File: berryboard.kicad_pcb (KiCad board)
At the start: 2 copper layers, 56 x 65 mm, 51 parts, among them J1 XT30_SERVO_PWR, J10 SERVO_7, J11 SERVO_8, J12 QWIIC_RPI_1, J13 QWIIC_RPI_2, J14 QWIIC_RPI_3, J15 QWIIC_MCU_1, J16 QWIIC_MCU_2, J17 QWIIC_MCU_3, J18 LEAK_1, J19 LEAK_2, J2 RPi_GPIO_40P, J20 HAT_5V_IN, J21 SWD, J3 USB_C_RP2350, J4 SERVO_1, J5 SERVO_2, J6 SERVO_3, J7 SERVO_4, J8 SERVO_5, J9 SERVO_6, U1 TPS2121, U2 AP2112K-3.3, U3 ICM-42688-P, U4 MMC5983MA, U5 24LC32, U6 RP2350B, U7 W25Q16JVSS

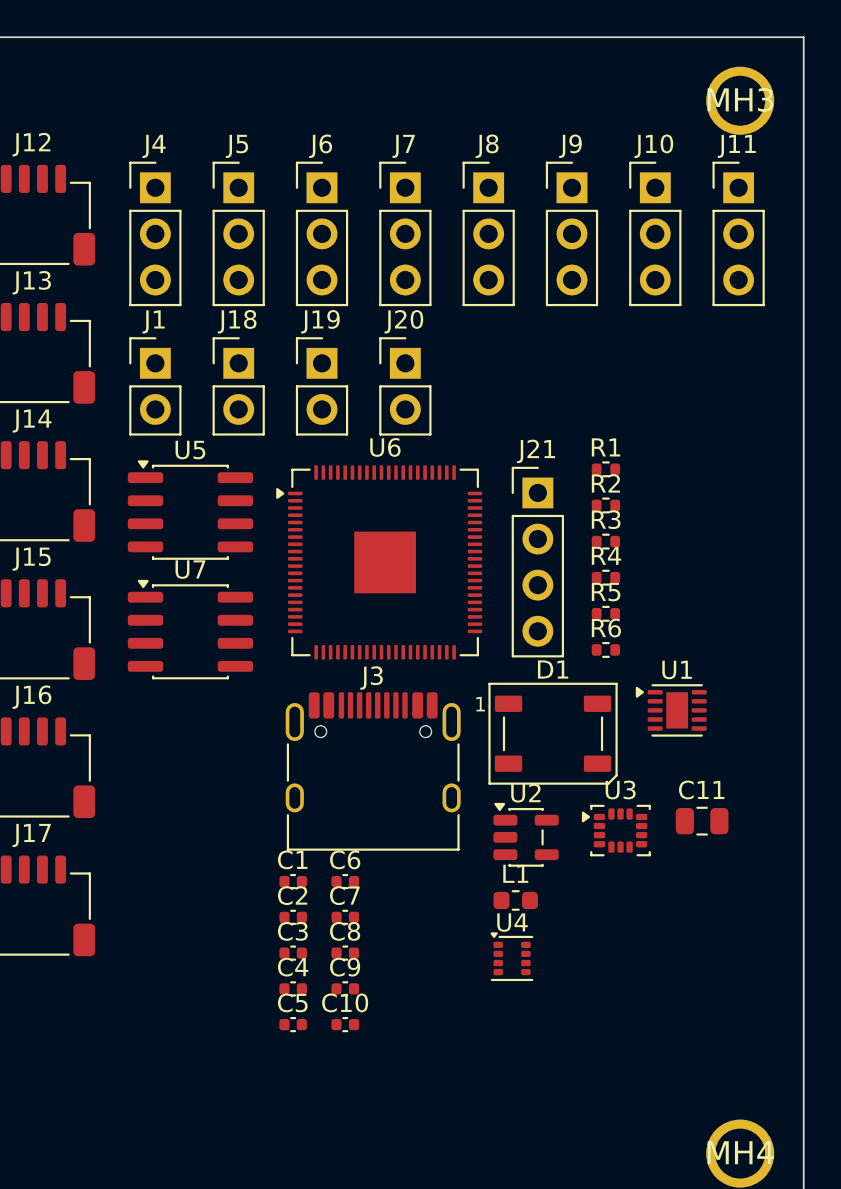
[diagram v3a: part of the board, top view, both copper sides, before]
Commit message: Update PCB: remove old servo connectors, add 3x 1x8 headers
Synced PCB from schematic after servo header redesign:
- Deleted J4–J11 footprints (eight 1x3 servo headers) from board
- Added J4 (SERVO_SIG), J5 (SERVO_PWR), J6 (SERVO_GND) as
  PinHeader_1x08_P2.54mm_Vertical footprints, ready for placement

Co-Authored-By: Claude Sonnet 4.6 <noreply@anthropic.com>
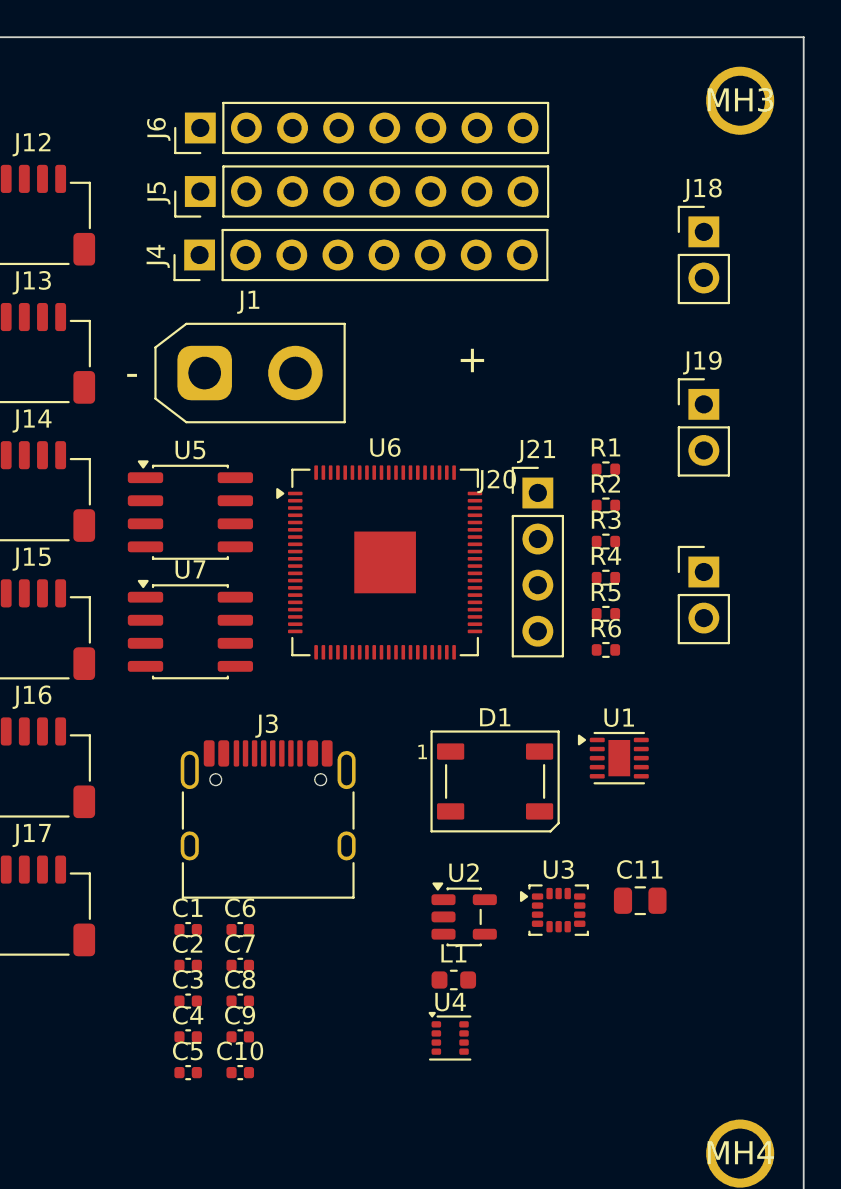
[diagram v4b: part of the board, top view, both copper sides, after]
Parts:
- removed J10: SERVO_7, Connector_PinHeader_2.54mm:PinHeader_1x03_P2.54mm_Vertical
- removed J11: SERVO_8, Connector_PinHeader_2.54mm:PinHeader_1x03_P2.54mm_Vertical
- removed J7: SERVO_4, Connector_PinHeader_2.54mm:PinHeader_1x03_P2.54mm_Vertical
- removed J8: SERVO_5, Connector_PinHeader_2.54mm:PinHeader_1x03_P2.54mm_Vertical
- removed J9: SERVO_6, Connector_PinHeader_2.54mm:PinHeader_1x03_P2.54mm_Vertical
- J1: footprint Connector_PinHeader_2.54mm:PinHeader_1x02_P2.54mm_Vertical -> Connector_AMASS:AMASS_XT30UPB-F_1x02_P5.0mm_Vertical
- J4: value SERVO_1 -> SERVO_SIG; footprint Connector_PinHeader_2.54mm:PinHeader_1x03_P2.54mm_Vertical -> Connector_PinHeader_2.54mm:PinHeader_1x08_P2.54mm_Vertical
- J5: value SERVO_2 -> SERVO_PWR; footprint Connector_PinHeader_2.54mm:PinHeader_1x03_P2.54mm_Vertical -> Connector_PinHeader_2.54mm:PinHeader_1x08_P2.54mm_Vertical
- J6: value SERVO_3 -> SERVO_GND; footprint Connector_PinHeader_2.54mm:PinHeader_1x03_P2.54mm_Vertical -> Connector_PinHeader_2.54mm:PinHeader_1x08_P2.54mm_Vertical
- moved J18 26.6 mm to (171.0, 83.2)
- moved J19 21.2 mm to (171.0, 92.7)
- moved J20 20.1 mm to (171.0, 102.0)
- moved J6 7.47 mm to (143.3, 77.5), turned to 90 degrees
- moved C1 6.36 mm to (142.6, 121.7)
- moved C10 6.36 mm to (145.5, 129.5)
- moved C2 6.36 mm to (142.6, 123.6)
- moved C3 6.36 mm to (142.6, 125.6)
- moved C4 6.36 mm to (142.6, 127.6)
- moved C5 6.36 mm to (142.6, 129.5)
- moved C6 6.36 mm to (145.5, 121.7)
- moved C7 6.36 mm to (145.5, 123.6)
- moved C8 6.36 mm to (145.5, 125.6)
- moved C9 6.36 mm to (145.5, 127.6)
- moved J3 6.36 mm to (147.0, 116.0)
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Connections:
- J4 pad 1: /SERVO_0 -> /SERVO_6
- J4 pad 2: /SERVO_PWR -> /SERVO_5
- J4 pad 3: /GND -> /SERVO_4
- J5 pad 1: /SERVO_1 -> /SERVO_PWR
- J5 pad 3: /GND -> /SERVO_PWR
- J6 pad 1: /SERVO_2 -> /GND
- J6 pad 2: /SERVO_PWR -> /GND

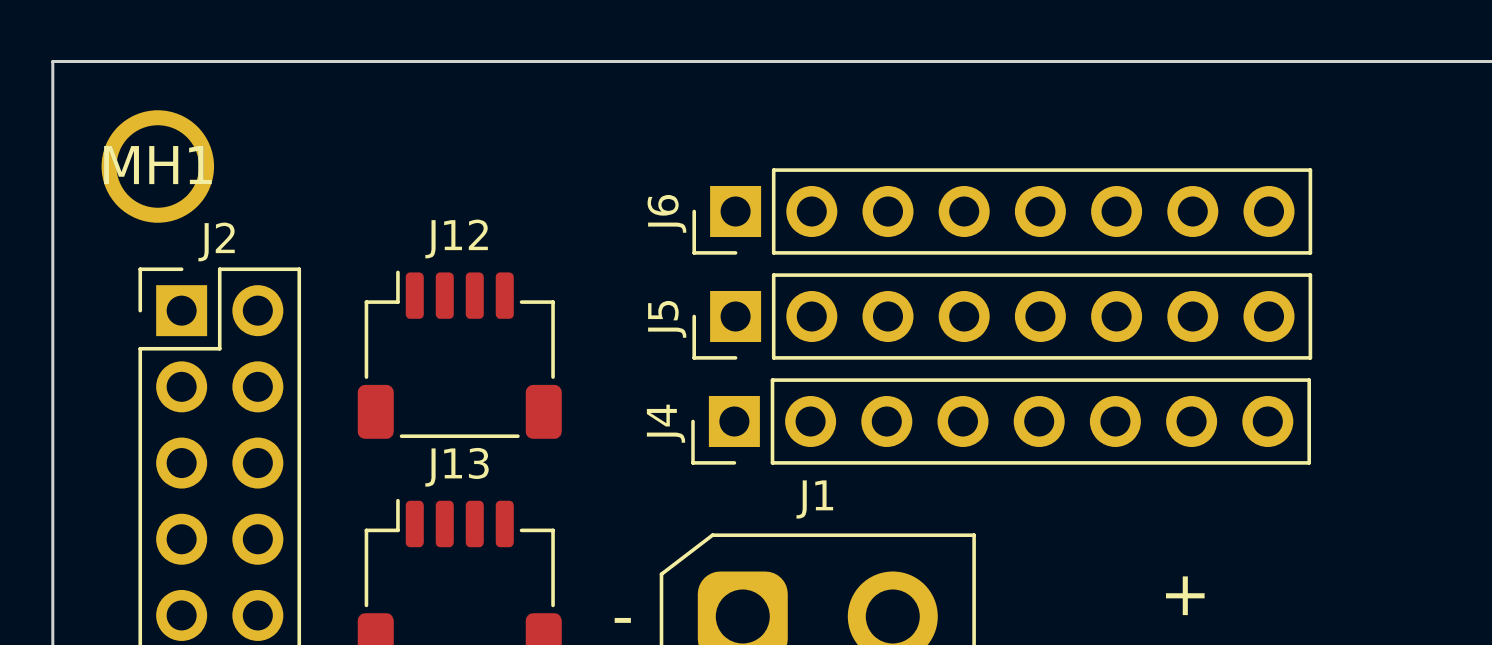
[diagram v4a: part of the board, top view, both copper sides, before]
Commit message: PCB: fix servo header spacing and order; schematic: add SERVO_PWR protection and SERVO_MON divider
PCB changes:
- Reorder J4/J5/J6 so signal (J4) is at top (y=77.5), power (J5) at y=80.04,
  ground (J6) at y=82.58 — matches yellow/red/black color convention
- Fix row spacing to exactly 2.54mm so a 3-pin Dupont housing mates all three
  rows simultaneously
- Align all three X coordinates to 143.22
- Add F.SilkS channel labels "1"–"8" above the servo header block

Schematic changes:
- Add D2 (SMBJ7.5A TVS diode) from SERVO_PWR to GND for transient protection
- Add C12 (100µF bulk capacitor) on SERVO_PWR for servo current decoupling
- Add R7/R8 (220k/100k) voltage divider: SERVO_PWR → SERVO_MON → GND,
  scaling up to 8.4V battery down to ≤2.6V for RP2350B ADC3 input
- U4 (MMC5983MA) footprint confirmed correct: OptoDevice:Broadcom_LGA-8_2x2mm_P0.5mm
  is the only matching 2×2mm / 0.5mm pitch LGA-8 in KiCad standard library
- U5 (24LC32) DNP flag confirmed already clear

Co-Authored-By: Claude Sonnet 4.6 <noreply@anthropic.com>
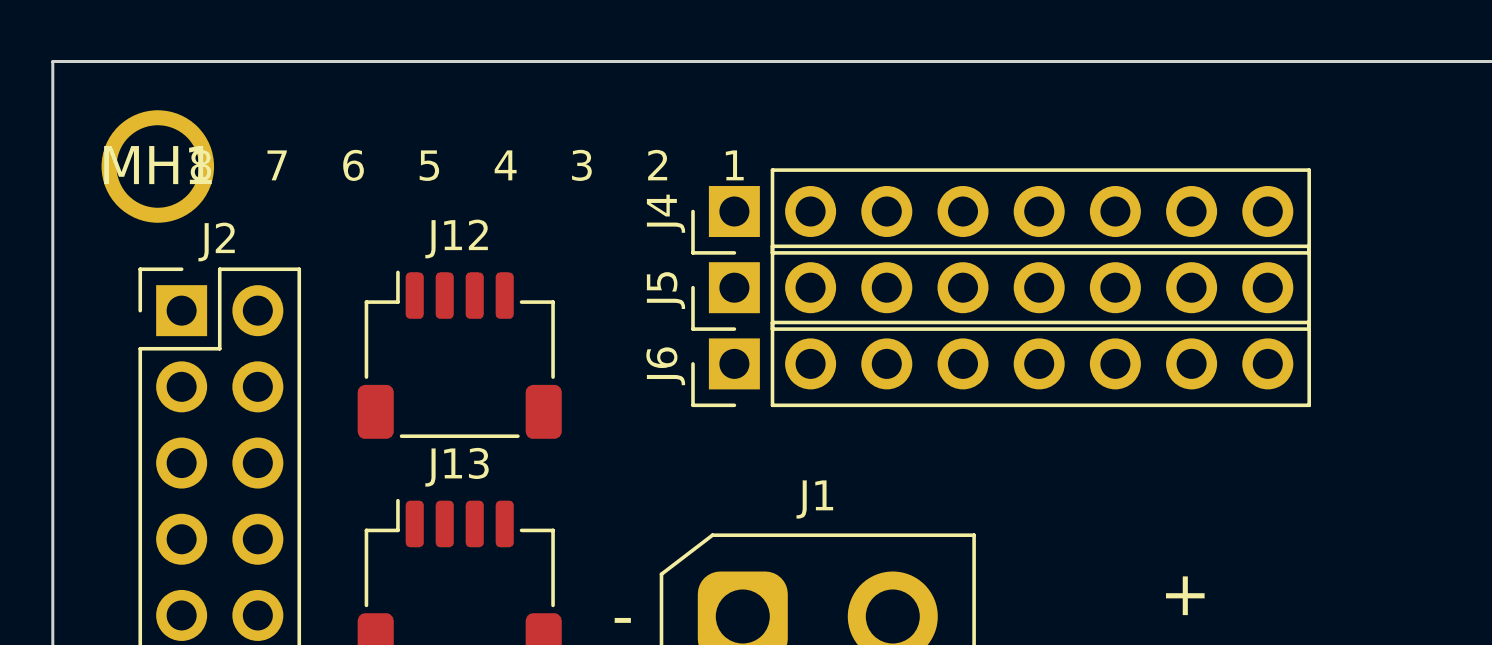
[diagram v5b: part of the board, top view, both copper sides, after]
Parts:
- moved J4 7.00 mm to (143.2, 77.5)
- moved J6 5.08 mm to (143.2, 82.6)
- moved J5 0.96 mm to (143.2, 80.0)
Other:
- board text added: "1"
- board text added: "2"
- board text added: "3"
- board text added: "4"
- board text added: "5"
- board text added: "6"
- board text added: "7"
- board text added: "8"
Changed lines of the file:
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@@
 	(footprint "Connector_PinHeader_2.54mm:PinHeader_1x08_P2.54mm_Vertical"
 		(layer "F.Cu")
-		(at 143.22 84.5 90)
+		(at 143.22 77.5 90)
 		(descr "Through hole straight pin header, 1x08, 2.54mm pitch, single row")
 		(tags "Through hole pin header THT 1x08 2.54mm single row")
@@
 	(footprint "Connector_PinHeader_2.54mm:PinHeader_1x08_P2.54mm_Vertical"
 		(layer "F.Cu")
-		(at 143.26 77.5 90)
+		(at 143.22 82.58 90)
 		(descr "Through hole straight pin header, 1x08, 2.54mm pitch, single row")
 		(tags "Through hole pin header THT 1x08 2.54mm single row")
@@
 	(footprint "Connector_PinHeader_2.54mm:PinHeader_1x08_P2.54mm_Vertical"
 		(layer "F.Cu")
-		(at 143.26 81 90)
+		(at 143.22 80.04 90)
 		(descr "Through hole straight pin header, 1x08, 2.54mm pitch, single row")
 		(tags "Through hole pin header THT 1x08 2.54mm single row")
@@
 		(layer "Edge.Cuts")
 	)
+	(gr_text "1"
+		(at 143.22 76)
+		(layer "F.SilkS")
+		(effects
+			(font
+				(size 1 1)
+				(thickness 0.15)
+			)
+			(justify center)
+		)
+	)
+	(gr_text "2"
+		(at 140.68 76)
+		(layer "F.SilkS")
+		(effects
+			(font
+				(size 1 1)
+				(thickness 0.15)
+			)
+			(justify center)
+		)
+	)
+	(gr_text "3"
+		(at 138.14 76)
+		(layer "F.SilkS")
+		(effects
+			(font
+				(size 1 1)
+				(thickness 0.15)
+			)
+			(justify center)
+		)
+	)
+	(gr_text "4"
+		(at 135.6 76)
+		(layer "F.SilkS")
+		(effects
+			(font
+				(size 1 1)
+				(thickness 0.15)
+			)
+			(justify center)
+		)
+	)
+	(gr_text "5"
+		(at 133.06 76)
+		(layer "F.SilkS")
+		(effects
+			(font
+				(size 1 1)
+				(thickness 0.15)
+			)
+			(justify center)
+		)
+	)
+	(gr_text "6"
+		(at 130.52 76)
+		(layer "F.SilkS")
+		(effects
+			(font
+				(size 1 1)
+				(thickness 0.15)
+			)
+			(justify center)
+		)
+	)
+	(gr_text "7"
+		(at 127.98 76)
+		(layer "F.SilkS")
+		(effects
+			(font
+				(size 1 1)
+				(thickness 0.15)
+			)
+			(justify center)
+		)
+	)
+	(gr_text "8"
+		(at 125.44 76)
+		(layer "F.SilkS")
+		(effects
+			(font
+				(size 1 1)
+				(thickness 0.15)
+			)
+			(justify center)
+		)
+	)
 	(embedded_fonts no)
